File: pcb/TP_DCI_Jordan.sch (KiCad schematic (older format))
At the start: 19 parts, among them J1 MICRO, J2 Display, SW1 SW_DIP_x03, U1 PCF8574

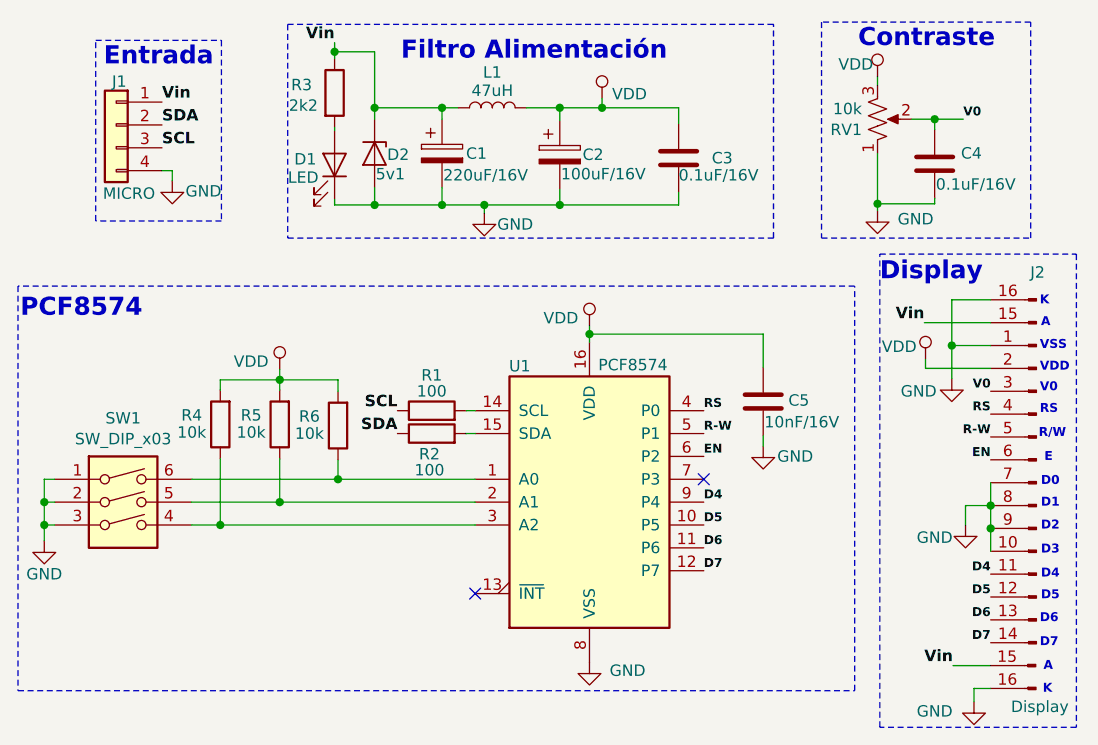
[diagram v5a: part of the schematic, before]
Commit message: asociación de huellas SMD recomendadas
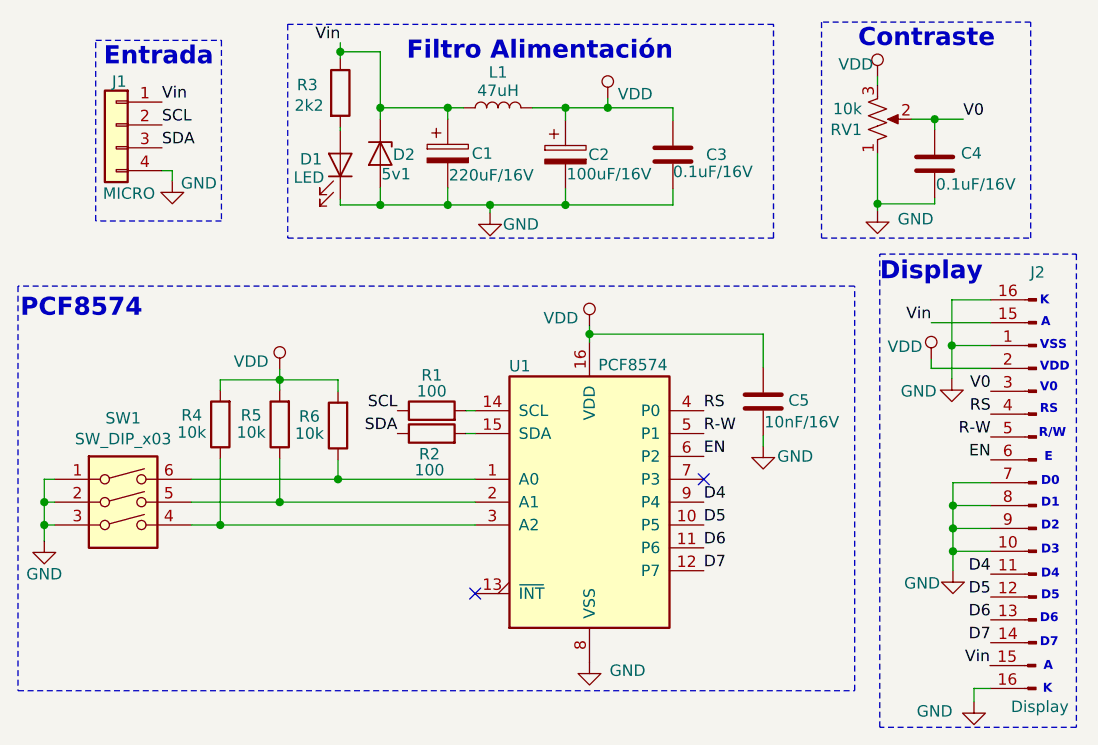
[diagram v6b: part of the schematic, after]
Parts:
- C1, C2: footprint miCapacitor_THT:Electrolitico_10uF -> Capacitor_SMD:CP_Elec_5x3.9
- D1: footprint LED_THT:LED_D3.0mm_Clear -> LED_SMD:LED_0805_2012Metric_Pad1.15x1.40mm_HandSolder
- D2: footprint miDiodo:miZener -> Diode_SMD:D_0805_2012Metric_Pad1.15x1.40mm_HandSolder
- J1: footprint Connector_Phoenix_MSTB:PhoenixContact_MSTBVA_2,5_4-G_1x04_P5.00mm_Vertical -> Connector_PinHeader_2.54mm:PinHeader_1x04_P2.54mm_Vertical
- L1: footprint Inductor_THT:L_Axial_L5.3mm_D2.2mm_P7.62mm_Horizontal_Vishay_IM-1 -> Inductor_SMD:L_0805_2012Metric_Pad1.15x1.40mm_HandSolder
- R1, R2, R3, R4, R5, R6: footprint Resistor_SMD:R_0805_2012Metric -> Resistor_SMD:R_0805_2012Metric_Pad1.15x1.40mm_HandSolder
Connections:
- net SCL: now also J1.2 (Pin_2); no longer J1.3 (Pin_3)
- net SDA: now also J1.3 (Pin_3); no longer J1.2 (Pin_2)
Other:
- moved on the sheet: C1, C2, C3, D1, D2, L1, R3
